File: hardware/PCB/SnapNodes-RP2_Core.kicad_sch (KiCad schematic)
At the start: 122 parts, among them J1 P_Female, J12 P_Female_Fallback, J13 P_Male_Fallback, J14 P_Female_Fallback, J15 P_Male_Fallback, J16 P_Female_Fallback, J17 P_Male_Fallback, J18 P_Female_Fallback, J19 P_Male_Fallback, J2 P_Male, J20 Conn_01x24_MountingPin, J3 P_Female, J4 P_Male, J5 P_Female, J6 P_Male, J7 P_Female, J8 P_Male, J9 SWD, Q1 2N7002W, U1 RP2350_80QFN, U2 TPS62A01PDDC, U3 BQ24232RGT, U4 ESP-PSRAM64H, U6 PY25Q128HA-SSH, U7 74AHC1G04, Y1 12M

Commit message: Hardware schematic revision
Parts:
- added R31, R32, R35, R36, R38, R39, R41, R42: 120, Resistor_SMD:R_0603_1608Metric, symbol Device:R_Small
- added R33, R37, R40, R43: 150, Resistor_SMD:R_0603_1608Metric, symbol Device:R_Small
- R1, R10, R4, R7: value 300 -> 150; Link https://www.lcsc.com/product-detail/C2930092.html -> (none)
- R11, R12, R2, R3, R5, R6, R8, R9: value 270 -> 120; Link https://www.lcsc.com/product-detail/C2907020.html -> (none)
- U6: value PY25Q128HA-SSH -> W25Q128JVSIQ; LCSC (none) -> C113767; Link https://www.lcsc.com/product-detail/C5354566.html -> (none)
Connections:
- net 3V3_EN_LATCH: no longer U1.23 (GPIO23)
- net BAT_ICHG_SAMPLE: no longer U1.57 (GPIO46_ADC6)
- net BAT_SAMPLE: no longer U1.58 (GPIO47_ADC7)
- net BAT_SAMPLE_EN: no longer U1.40 (GPIO32)
- net BAT_~{CHG}: no longer U1.14 (GPIO15)
- net PA.CA: no longer U1.7 (GPIO9)
- net PA.CB: now also R33.2; no longer D11.1 (K), J1.4 (Pin_4), J12.4 (Pin_4), U1.13 (GPIO14)
- net PA.D0: now also R31.2; no longer D7.1 (K), J13.3 (Pin_3), J2.3 (Pin_3), U1.8 (GPIO10)
- net PA.D1: no longer U1.9 (GPIO11)
- net PA.D2: now also R32.2; no longer D9.1 (K), J1.2 (Pin_2), J12.2 (Pin_2), U1.11 (GPIO12)
- net PA.D3: no longer U1.12 (GPIO13)
- net PB.CA: no longer U1.17 (GPIO17)
- net PB.CB: now also R40.2; no longer D23.1 (K), J16.4 (Pin_4), J3.4 (Pin_4), U1.22 (GPIO22)
- net PB.D0: now also R38.2; no longer D19.1 (K), J17.3 (Pin_3), J4.3 (Pin_3), U1.18 (GPIO18)
- net PB.D1: no longer U1.19 (GPIO19)
- net PB.D2: now also R39.2; no longer D21.1 (K), J16.2 (Pin_2), J3.2 (Pin_2), U1.20 (GPIO20)
- net PB.D3: no longer U1.21 (GPIO21)
- net PC.CA: no longer U1.26 (GPIO25)
- net PC.CB: now also R37.2; no longer D17.1 (K), J14.4 (Pin_4), J5.4 (Pin_4), U1.38 (GPIO30)
- net PC.D0: now also R35.2; no longer D13.1 (K), J15.3 (Pin_3), J6.3 (Pin_3), U1.27 (GPIO26)
- net PC.D1: no longer U1.28 (GPIO27)
- net PC.D2: now also R36.2; no longer D15.1 (K), J14.2 (Pin_2), J5.2 (Pin_2), U1.36 (GPIO28)
- net PC.D3: no longer U1.37 (GPIO29)
- net PD.CA: no longer U1.79 (GPIO2)
- net PD.CB: now also R43.2; no longer D29.1 (K), J18.4 (Pin_4), J7.4 (Pin_4), U1.4 (GPIO7)
- net PD.D0: now also R41.2; no longer D25.1 (K), J19.3 (Pin_3), J8.3 (Pin_3), U1.80 (GPIO3)
- net PD.D1: no longer U1.1 (GPIO4)
- net PD.D2: now also R42.2; no longer D27.1 (K), J18.2 (Pin_2), J7.2 (Pin_2), U1.2 (GPIO5)
- net PD.D3: no longer U1.3 (GPIO6)
- net at D5.1 (K), R23.2: no longer U1.39 (GPIO31)
- net GPIO0: no longer names the net of U1.42 (GPIO33)
- net GPIO1: no longer names the net of U1.43 (GPIO34)
- net GPIO10: no longer names the net of U1.54 (GPIO43_ADC3)
- net GPIO11: no longer names the net of U1.55 (GPIO44_ADC4)
- net GPIO12: no longer names the net of U1.56 (GPIO45_ADC5)
- net GPIO2: no longer names the net of U1.44 (GPIO35)
- net GPIO3: no longer names the net of U1.45 (GPIO36)
- net GPIO4: no longer names the net of U1.46 (GPIO37)
- net GPIO5: no longer names the net of U1.47 (GPIO38)
- net GPIO6: no longer names the net of U1.48 (GPIO39)
- net GPIO7: no longer names the net of U1.49 (GPIO40_ADC0)
- net GPIO8: no longer names the net of U1.52 (GPIO41_ADC1)
- net GPIO9: no longer names the net of U1.53 (GPIO42_ADC2)
- net PA.CAR: no longer names the net of D6.1 (K), J13.4 (Pin_4), J2.2 (Pin_2), R1.1
- net PA.CAR: no longer U1.6 (GPIO8)
- net PB.CAR: no longer names the net of D18.1 (K), J17.4 (Pin_4), J4.2 (Pin_2), R4.1
- net PB.CAR: no longer U1.16 (GPIO16)
- net PC.CAR: no longer names the net of D12.1 (K), J15.4 (Pin_4), J6.2 (Pin_2), R7.1
- net PC.CAR: no longer U1.25 (GPIO24)
- net PD.CAR: no longer names the net of D24.1 (K), J19.4 (Pin_4), J8.2 (Pin_2), R10.1
- net PD.CAR: no longer U1.78 (GPIO1)
- new net: D7.1 (K), J13.3 (Pin_3), J2.3 (Pin_3), R31.1
- new net: D9.1 (K), J1.2 (Pin_2), J12.2 (Pin_2), R32.1
- new net: D11.1 (K), J1.4 (Pin_4), J12.4 (Pin_4), R33.1
- new net: D21.1 (K), J16.2 (Pin_2), J3.2 (Pin_2), R39.1
- new net: D23.1 (K), J16.4 (Pin_4), J3.4 (Pin_4), R40.1
- new net: D29.1 (K), J18.4 (Pin_4), J7.4 (Pin_4), R43.1
- new net: D25.1 (K), J19.3 (Pin_3), J8.3 (Pin_3), R41.1
- new net: D13.1 (K), J15.3 (Pin_3), J6.3 (Pin_3), R35.1
- new net: D15.1 (K), J14.2 (Pin_2), J5.2 (Pin_2), R36.1
- new net: D17.1 (K), J14.4 (Pin_4), J5.4 (Pin_4), R37.1
- new net: D27.1 (K), J18.2 (Pin_2), J7.2 (Pin_2), R42.1
- new net: D19.1 (K), J17.3 (Pin_3), J4.3 (Pin_3), R38.1
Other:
- note added: "Keep these on ADC Pins"
- note added: "QMI_CS1 must be on GPIO0"
- note added: "Route remaining GPIOs to the inter-board FPC connector, give it as many ADC pins as possible."
- moved on the sheet: D5

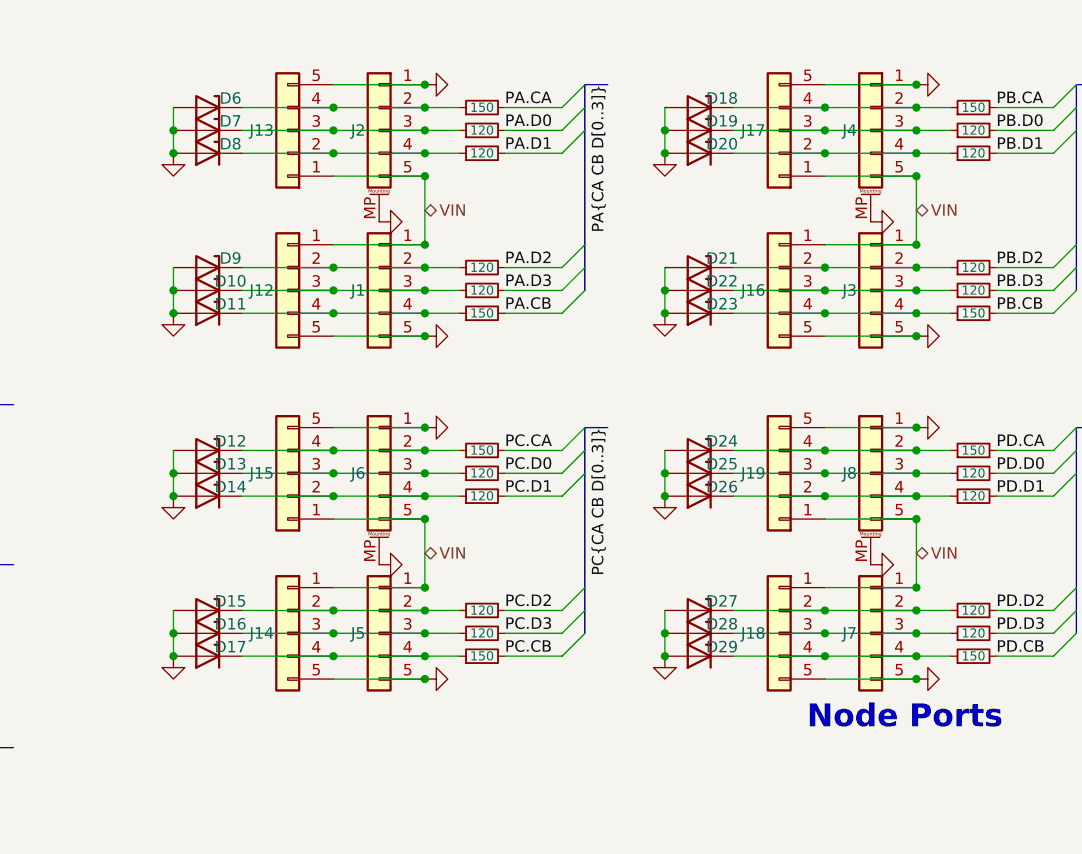
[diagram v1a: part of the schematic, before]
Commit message: Schematic: remove fallback connectors
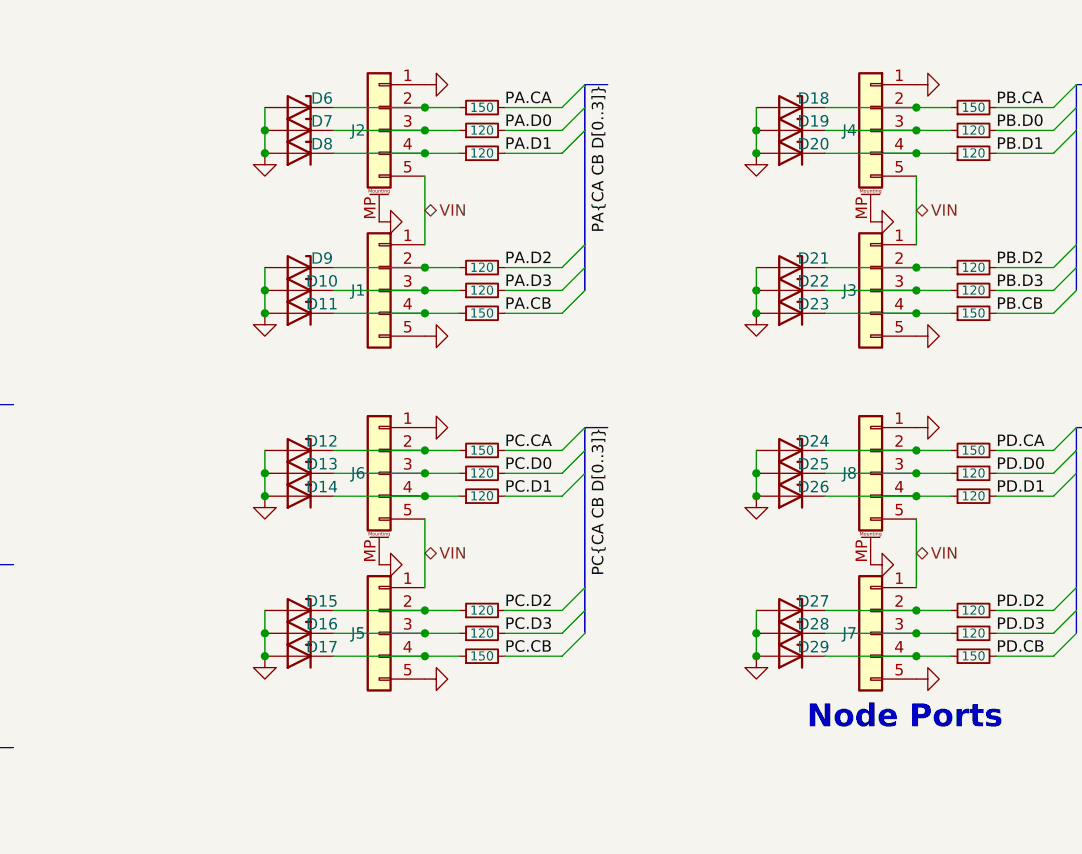
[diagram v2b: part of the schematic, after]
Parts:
- removed J12, J14, J16, J18: P_Female_Fallback, Project:PinSocket_1x05_P2.54mm_Horizontal_NoSilk, symbol Connector_Generic:Conn_01x05
- removed J13, J15, J17, J19: P_Male_Fallback, Project:PinHeader_1x05_P2.54mm_Horizontal_NoSilk, symbol Connector_Generic:Conn_01x05
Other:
- moved on the sheet: D10, D11, D12, D13, D14, D15, D16, D17, D18, D19, D20, D21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

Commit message: SnapNode-RP2 Core V2 PCB
Signed-off-by: Hanxiang Chen <jhxchen7@outlook.com>
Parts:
- removed BT1: LIR2450, Project:BS-24-B___014, symbol Device:Battery_Cell
- removed D10, D11, D12, D13, D14, D15, D16, D17, D18, D19, D20, D21, D22, D23, D24, D25, D26, D27, D28, D29, D6, D7, D8, D9: ESD5Z3.3-HXY, Diode_SMD:D_SOD-523, symbol Diode:ESD5Zxx
- added BT1: 702, Connector_Molex:Molex_PicoBlade_53261-0271_1x02-1MP_P1.25mm_Horizontal, symbol Connector_Generic_MountingPin:Conn_01x02_MountingPin
- added D10, D11, D12, D13, D14, D15, D16, D17, D18, D19, D20, D21, D22, D23, D24, D25, D26, D27, D28, D3, D6, D7, D8, D9: PESD3V3S1BA, Diode_SMD:D_SOD-523, symbol Diode:PESD3V3S1UL
- added TP2, TP3, TP4, TP5: TestPoint, TestPoint:TestPoint_Pad_D1.0mm, symbol Connector:TestPoint
- C1, C3: footprint Capacitor_SMD:C_0402_1005Metric -> RP2350:C_0402_1005Metric_small_pads
- C37, C4, C5, C6, C7, C8: footprint Capacitor_SMD:C_0603_1608Metric -> Capacitor_SMD:C_0402_1005Metric
- J9: footprint Connector_JST:JST_SH_BM03B-SRSS-TB_1x03-1MP_P1.00mm_Vertical -> Connector_JST:JST_SH_SM03B-SRSS-TB_1x03-1MP_P1.00mm_Horizontal
- JP2: now left out of the parts list
- R1, R10, R11, R12, R14, R15, R16, R2, R28, R29, R3, R30, R31, R32, R33, R34, R35, R36, R37, R38, R39, R4, R40, R41, R42, R43, R5, R6, R7, R8, R9: footprint Resistor_SMD:R_0603_1608Metric -> Resistor_SMD:R_0402_1005Metric
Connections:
- net BTN_CENTER_VBUS is gone; now on net BTN_CENTER: D1.2 (A)
- net GND_CORE is gone; now on net GND: C1.2, C10.2, C11.2, C12.2, C13.2, C14.2, C15.2, C16.2, C17.2, C18.2, C19.2, C2.2, C20.2, C21.2, C22.2, C23.1, C24.1, C25.2, C26.2, C3.2, C37.2, C4.2, C5.2, C6.1, C7.2, C8.2, C9.2, D5.2 (A), J1.5 (Pin_5), J2.1 (Pin_1), J2.MP (MountPin), J3.5 (Pin_5), J4.1 (Pin_1), J4.MP (MountPin), J5.5 (Pin_5), J6.1 (Pin_1), J6.MP (MountPin), J7.5 (Pin_5), J8.1 (Pin_1), J8.MP (MountPin), J9.2 (Pin_2), JP2.1 (A), Q1.2 (S), R14.1, R15.1, R16.2, R19.1, R20.1, R34.1, U1.62 (VREG_PGND), U1.81 (GND), U2.2 (GND), U3.17 (VSS), U3.4 (CE), U3.5 (EN2), U3.8 (VSS), U4.4 (VSS), U6.4 (GND), U7.3 (GND), Y1.2, Y1.4
- net +3V3: now also J20.5 (Pin_5)
- net +BATT: now also BT1.2 (Pin_2)
- net 3V3_EN_LATCH: now also U1.38 (GPIO30)
- net BAT_ICHG_SAMPLE: now also U1.57 (GPIO46_ADC6)
- net BAT_SAMPLE: now also U1.58 (GPIO47_ADC7)
- net BAT_SAMPLE_EN: now also U1.40 (GPIO32)
- net BAT_~{CHG}: now also U1.19 (GPIO19)
- net PA.CA: now also U1.4 (GPIO7)
- net PA.CB: now also U1.11 (GPIO12)
- net PA.D0: now also U1.6 (GPIO8)
- net PA.D1: now also U1.7 (GPIO9)
- net PA.D2: now also U1.8 (GPIO10)
- net PA.D3: now also U1.9 (GPIO11)
- net PB.CA: now also U1.12 (GPIO13)
- net PB.CB: now also U1.18 (GPIO18)
- net PB.D0: now also U1.13 (GPIO14)
- net PB.D1: now also U1.14 (GPIO15)
- net PB.D2: now also U1.16 (GPIO16)
- net PB.D3: now also U1.17 (GPIO17)
- net PC.CA: now also U1.20 (GPIO20)
- net PC.CB: now also U1.26 (GPIO25)
- net PC.D0: now also U1.21 (GPIO21)
- net PC.D1: now also U1.22 (GPIO22)
- net PC.D2: now also U1.23 (GPIO23)
- net PC.D3: now also U1.25 (GPIO24)
- net PD.CA: now also U1.78 (GPIO1)
- net PD.CB: now also U1.3 (GPIO6)
- net PD.D0: now also U1.79 (GPIO2)
- net PD.D1: now also U1.80 (GPIO3)
- net PD.D2: now also U1.1 (GPIO4)
- net PD.D3: now also U1.2 (GPIO5)
- net USB_D+: now also J20.3 (Pin_3)
- net USB_D-: now also J20.2 (Pin_2)
- net VBUS: now also J20.22 (Pin_22)
- net VIN: now also J20.20 (Pin_20), J20.21 (Pin_21)
- net at J3.3 (Pin_3), R6.1: now also D21.1 (K)
- net at J7.4 (Pin_4), R43.1: now also D28.1 (K)
- net at J3.2 (Pin_2), R39.1: now also D20.1 (K)
- net at D5.1 (K), R23.2: now also U1.39 (GPIO31)
- net at J1.2 (Pin_2), R32.1: now also D8.1 (K)
- net at J4.2 (Pin_2), R4.1: now also D17.1 (K)
- net at J8.3 (Pin_3), R41.1: now also D24.1 (K)
- net at J2.4 (Pin_4), R2.1: now also D7.1 (K)
- net at J4.4 (Pin_4), R5.1: now also D19.1 (K)
- net at J3.4 (Pin_4), R40.1: now also D22.1 (K)
- net at J8.2 (Pin_2), R10.1: now also D23.1 (K)
- net GPIO26: now reaches U1.27 (GPIO26)
- net GPIO26: now also TP2.1
- net GPIO27: now reaches U1.28 (GPIO27)
- net GPIO27: now also TP3.1
- net GPIO28: now reaches U1.36 (GPIO28)
- net GPIO28: now also TP4.1
- net GPIO29: now reaches U1.37 (GPIO29)
- net GPIO29: now also TP5.1
- net GPIO0: now reaches U1.42 (GPIO33)
- net GPIO0: now also J20.19 (Pin_19)
- net GPIO1: now reaches U1.43 (GPIO34)
- net GPIO1: now also J20.18 (Pin_18)
- net GPIO2: now reaches U1.44 (GPIO35)
- net GPIO2: now also J20.17 (Pin_17)
- net GPIO3: now reaches U1.45 (GPIO36)
- net GPIO3: now also J20.16 (Pin_16)
- net GPIO4: now reaches U1.46 (GPIO37)
- net GPIO4: now also J20.15 (Pin_15)
- net GPIO5: now reaches U1.47 (GPIO38)
- net GPIO5: now also J20.14 (Pin_14)
- net GPIO6: now reaches U1.48 (GPIO39)
- net GPIO6: now also J20.13 (Pin_13)
- net GPIO7: now reaches U1.49 (GPIO40_ADC0)
- net GPIO7: now also J20.12 (Pin_12)
- net GPIO8: now reaches U1.52 (GPIO41_ADC1)
- net GPIO8: now also J20.11 (Pin_11)
- net GPIO9: now reaches U1.53 (GPIO42_ADC2)
- net GPIO9: now also J20.10 (Pin_10)
- net GPIO10: now reaches U1.54 (GPIO43_ADC3)
- net GPIO10: now also J20.9 (Pin_9)
- net GPIO11: now reaches U1.55 (GPIO44_ADC4)
- net GPIO11: now also J20.8 (Pin_8)
- net GPIO12: now reaches U1.56 (GPIO45_ADC5)
- net GPIO12: now also J20.7 (Pin_7)
- net at J8.4 (Pin_4), R11.1: now also D25.1 (K)
- net at J7.3 (Pin_3), R12.1: now also D27.1 (K)
- net at J5.3 (Pin_3), R9.1: now also D15.1 (K)
- net at J6.3 (Pin_3), R35.1: now also D12.1 (K)
- net GND: now reaches J20.1 (Pin_1)
- net GND: now also J20.24 (Pin_24), J20.4 (Pin_4), J20.6 (Pin_6), J20.MP (MountPin), BT1.1 (Pin_1), BT1.MP (MountPin), D10.2 (A), D11.2 (A), D12.2 (A), D13.2 (A), D14.2 (A), D15.2 (A), D16.2 (A), D17.2 (A), D18.2 (A), D19.2 (A), D20.2 (A), D21.2 (A), D22.2 (A), D23.2 (A), D24.2 (A), D25.2 (A), D26.2 (A), D27.2 (A), D28.2 (A), D3.2 (A), D6.2 (A), D7.2 (A), D8.2 (A), D9.2 (A)
- net BTN_CENTER: now reaches J20.23 (Pin_23)
- net at J5.2 (Pin_2), R36.1: now also D14.1 (K)
- net at J1.3 (Pin_3), R3.1: now also D9.1 (K)
- net at J5.4 (Pin_4), R37.1: now also D16.1 (K)
- net at J1.4 (Pin_4), R33.1: now also D10.1 (K)
- net at J6.4 (Pin_4), R8.1: now also D13.1 (K)
- net at J2.2 (Pin_2), R1.1: now also D3.1 (K)
- net at J7.2 (Pin_2), R42.1: now also D26.1 (K)
- net at J2.3 (Pin_3), R31.1: now also D6.1 (K)
- net at J4.3 (Pin_3), R38.1: now also D18.1 (K)
- net at J6.2 (Pin_2), R7.1: now also D11.1 (K)
- net SWD renamed SWDIO
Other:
- company: (none) -> Hang Su & Jason Chen
- title: (none) -> SnapNode RP2 Core

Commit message: HAT V2 PCB done, minor fix for Core PCB
Signed-off-by: Hanxiang Chen <jhxchen7@outlook.com>
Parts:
- added D29, D30, D31, D32: PESD5V0S1BA, Diode_SMD:D_SOD-523, symbol Diode:PESD3V3S1UL
- added D33, D34: PESD3V3S1BA, Diode_SMD:D_SOD-523, symbol Diode:PESD3V3S1UL
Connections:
- net GND: now also D29.2 (A), D30.2 (A), D31.2 (A), D32.2 (A), D33.2 (A), D34.2 (A)
- net PA.CA: now also D3.1 (K)
- net PA.CB: now also D10.1 (K)
- net PA.D0: now also D6.1 (K)
- net PA.D1: now also D7.1 (K)
- net PA.D2: now also D8.1 (K)
- net PA.D3: now also D9.1 (K)
- net PB.CA: now also D17.1 (K)
- net PB.CB: now also D22.1 (K)
- net PB.D0: now also D18.1 (K)
- net PB.D1: now also D19.1 (K)
- net PB.D2: now also D20.1 (K)
- net PB.D3: now also D21.1 (K)
- net PC.CA: now also D11.1 (K)
- net PC.CB: now also D16.1 (K)
- net PC.D0: now also D12.1 (K)
- net PC.D1: now also D13.1 (K)
- net PC.D2: now also D14.1 (K)
- net PC.D3: now also D15.1 (K)
- net PD.CA: now also D23.1 (K)
- net PD.CB: now also D28.1 (K)
- net PD.D0: now also D24.1 (K)
- net PD.D1: now also D25.1 (K)
- net PD.D2: now also D26.1 (K)
- net PD.D3: now also D27.1 (K)
- net SWCLK: now also D33.1 (K)
- net SWDIO: now also D34.1 (K)
- net VIN: now also D29.1 (K), D30.1 (K), D31.1 (K), D32.1 (K)
- net at J5.2 (Pin_2), R36.1: no longer D14.1 (K)
- net at J4.4 (Pin_4), R5.1: no longer D19.1 (K)
- net at J7.4 (Pin_4), R43.1: no longer D28.1 (K)
- net at J3.2 (Pin_2), R39.1: no longer D20.1 (K)
- net at J4.2 (Pin_2), R4.1: no longer D17.1 (K)
- net at J8.3 (Pin_3), R41.1: no longer D24.1 (K)
- net at J4.3 (Pin_3), R38.1: no longer D18.1 (K)
- net at J8.2 (Pin_2), R10.1: no longer D23.1 (K)
- net at J6.3 (Pin_3), R35.1: no longer D12.1 (K)
- net at J2.4 (Pin_4), R2.1: no longer D7.1 (K)
- net at J3.3 (Pin_3), R6.1: no longer D21.1 (K)
- net at J3.4 (Pin_4), R40.1: no longer D22.1 (K)
- net at J5.3 (Pin_3), R9.1: no longer D15.1 (K)
- net at J1.2 (Pin_2), R32.1: no longer D8.1 (K)
- net at J8.4 (Pin_4), R11.1: no longer D25.1 (K)
- net at J7.2 (Pin_2), R42.1: no longer D26.1 (K)
- net at J5.4 (Pin_4), R37.1: no longer D16.1 (K)
- net at J1.3 (Pin_3), R3.1: no longer D9.1 (K)
- net at J6.4 (Pin_4), R8.1: no longer D13.1 (K)
- net at J1.4 (Pin_4), R33.1: no longer D10.1 (K)
- net at J2.3 (Pin_3), R31.1: no longer D6.1 (K)
- net at J2.2 (Pin_2), R1.1: no longer D3.1 (K)
- net at J7.3 (Pin_3), R12.1: no longer D27.1 (K)
- net at J6.2 (Pin_2), R7.1: no longer D11.1 (K)
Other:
- note added: "Daughter Board"
- company: Hang Su & Jason Chen -> shBLOCK & Jason Chen
- moved on the sheet: D10, D11, D12, D13, D14, D15, D16, D17, D18, D19, D20, D21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

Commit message: all V2 PCBs done
Signed-off-by: Hanxiang Chen <jhxchen7@outlook.com>
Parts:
- BT1: LCSC P/N (none) -> C53477378
- C1, C12, C2, C3, C4, C5, C6, C7, C9: LCSC P/N (none) -> C19666
- C10, C11, C13, C14, C15, C16, C17, C18, C19, C20, C21, C22, C25, C26, C37: LCSC P/N (none) -> C1525
- C23, C24: LCSC P/N (none) -> C1548
- C36: LCSC P/N (none) -> C106996
- C8: footprint Capacitor_SMD:C_0402_1005Metric -> Capacitor_SMD:C_0805_2012Metric; LCSC P/N (none) -> C45783
- D1, D2, D4: LCSC P/N (none) -> C7420320
- D10, D11, D12, D13, D14, D15, D16, D17, D18, D19, D20, D21, D22, D23, D24, D25, D26, D27, D28, D3, D33, D34, D6, D7, D8, D9: LCSC P/N (none) -> C46550846
- D29, D30, D31, D32: LCSC P/N (none) -> C5158048
- D5: LCSC P/N (none) -> C2910134
- J20: LCSC P/N (none) -> C481246
- J9: LCSC P/N (none) -> C7430445
- L1: LCSC P/N (none) -> C42411119
- L2: LCSC P/N (none) -> C7471163
- Q1: LCSC P/N (none) -> C7420322
- R1, R10, R33, R37, R4, R40, R43, R7: LCSC P/N (none) -> C25082
- R11, R12, R2, R3, R31, R32, R35, R36, R38, R39, R41, R42, R5, R6, R8, R9: LCSC P/N (none) -> C25079
- R13, R24: LCSC P/N (none) -> C25105
- R14, R15, R17, R18: LCSC P/N (none) -> C25744
- R16: LCSC P/N (none) -> C25871
- R19, R22, R23, R28, R29, R34: LCSC P/N (none) -> C25741
- R20: LCSC P/N (none) -> C19709
- R21: LCSC P/N (none) -> C163467
- R25, R30: LCSC P/N (none) -> C11702
- R26, R27: LCSC P/N (none) -> C25100
- U1: LCSC P/N (none) -> C42415655
- U2: LCSC P/N (none) -> C42267816
- U3: LCSC P/N (none) -> C528622
- U7: LCSC P/N (none) -> C52140422
- Y1: LCSC P/N (none) -> C50430
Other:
- title: SnapNode RP2 Core -> SnapNodes RP2 Core

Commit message: changed LCSC P/N of 5V TVS, moved a MLCC that conflicts with FPC connector on core board
Signed-off-by: Hanxiang Chen <jhxchen7@outlook.com>
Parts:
- D29, D30, D31, D32: LCSC P/N C5158048 -> C314264
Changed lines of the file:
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@@
 			)
 		)
-		(property "LCSC P/N" "C5158048"
+		(property "LCSC P/N" "C314264"
 			(at 236.22 21.59 0)
 			(hide yes)
@@
 			)
 		)
-		(property "LCSC P/N" "C5158048"
+		(property "LCSC P/N" "C314264"
 			(at 256.54 21.59 0)
 			(hide yes)
@@
 			)
 		)
-		(property "LCSC P/N" "C5158048"
+		(property "LCSC P/N" "C314264"
 			(at 275.59 21.59 0)
 			(hide yes)
@@
 			)
 		)
-		(property "LCSC P/N" "C5158048"
+		(property "LCSC P/N" "C314264"
 			(at 295.91 21.59 0)
 			(hide yes)
